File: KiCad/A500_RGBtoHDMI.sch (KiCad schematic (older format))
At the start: 3 parts, among them J1 Conn_02x20_Odd_Even, U1 Denise_MB_pins, U2 Denise_SocketOnAdapter

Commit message: improved design
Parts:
- U1: value Denise_MB_pins -> Denise_MB_PinHeader
- U2: value Denise_SocketOnAdapter -> Denise_MB_PinSocket
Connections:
- net D6: now reaches U1.1 (D6)
- net D6: now also U2.1 (D6)
- net D5: now reaches U1.2 (D5)
- net D5: now also U2.2 (D5)
- net D4: now reaches U1.3 (D4)
- net D4: now also U2.3 (D4)
- net D3: now reaches U1.4 (D3)
- net D3: now also U2.4 (D3)
- net D2: now reaches U1.5 (D2)
- net D2: now also U2.5 (D2)
- net D1: now reaches U1.6 (D1)
- net D1: now also U2.6 (D1)
- net D0: now reaches U1.7 (D0)
- net D0: now also U2.7 (D0)
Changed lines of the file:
@@
 P 2950 3100
 F 0 "U1" H 2950 4665 50  0000 C CNN
-F 1 "Denise_MB_pins" H 2950 4574 50  0000 C CNN
+F 1 "Denise_MB_PinHeader" H 2950 4574 50  0000 C CNN
 F 2 "Package_DIP:DIP-48_W15.24mm_LongPads" H 2900 1600 50  0001 C CNN
 F 3 "" H 2900 1600 50  0001 C CNN
@@
 $Comp
 L A500_RGBtoHDMI:Denise U2
-U 1 1 623C9B51
-P 4950 3100
-F 0 "U2" H 4950 4665 50  0000 C CNN
-F 1 "Denise_SocketOnAdapter" H 4950 4574 50  0000 C CNN
-F 2 "Package_DIP:DIP-48_W15.24mm_Socket_LongPads" H 4900 1600 50  0001 C CNN
-F 3 "" H 4900 1600 50  0001 C CNN
-	1    4950 3100
+U 1 1 623E379A
+P 4700 3100
+F 0 "U2" H 4700 4665 50  0000 C CNN
+F 1 "Denise_MB_PinSocket" H 4700 4574 50  0000 C CNN
+F 2 "Package_DIP:DIP-48_W15.24mm_Socket_LongPads" H 4650 1600 50  0001 C CNN
+F 3 "" H 4650 1600 50  0001 C CNN
+	1    4700 3100
 	1    0    0    -1
 $EndComp
+Text GLabel 2400 1800 0    50   BiDi ~ 0
+D6
+Text GLabel 4150 1800 0    50   BiDi ~ 0
+D6
+Text GLabel 2400 1900 0    50   BiDi ~ 0
+D5
+Text GLabel 4150 1900 0    50   BiDi ~ 0
+D5
+Text GLabel 2400 2000 0    50   BiDi ~ 0
+D4
+Text GLabel 2400 2100 0    50   BiDi ~ 0
+D3
+Text GLabel 2400 2200 0    50   BiDi ~ 0
+D2
+Text GLabel 2400 2300 0    50   BiDi ~ 0
+D1
+Text GLabel 2400 2400 0    50   BiDi ~ 0
+D0
+Text GLabel 4150 2000 0    50   BiDi ~ 0
+D4
+Text GLabel 4150 2100 0    50   BiDi ~ 0
+D3
+Text GLabel 4150 2200 0    50   BiDi ~ 0
+D2
+Text GLabel 4150 2300 0    50   BiDi ~ 0
+D1
+Text GLabel 4150 2400 0    50   BiDi ~ 0
+D0
 $EndSCHEMATC

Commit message: more routing
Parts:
- U2: value Denise_MB_PinSocket -> Denise_Socket
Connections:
- net +5V: now also U1.19 (VCC), U2.19 (VCC); no longer J1.1 (Pin_1)
- net GND: now also U1.37 (GND), U2.37 (GND); no longer J1.2 (Pin_2)
- net RGA8: now reaches U1.10 (RGA8)
- net RGA8: now also U2.10 (RGA8)
- net RGA7: now reaches U1.11 (RGA7)
- net RGA7: now also U2.11 (RGA7)
- net RGA6: now reaches U1.12 (RGA6)
- net RGA6: now also U2.12 (RGA6)
- net RGA5: now reaches U1.13 (RGA5)
- net RGA5: now also U2.13 (RGA5)
- net RGA4: now reaches U1.14 (RGA4)
- net RGA4: now also U2.14 (RGA4)
- net RGA3: now reaches U1.15 (RGA3)
- net RGA3: now also U2.15 (RGA3)
- net RGA2: now reaches U1.16 (RGA2)
- net RGA2: now also U2.16 (RGA2)
- net RGA1: now reaches U1.17 (RGA1)
- net RGA1: now also U2.17 (RGA1)
- net BURST: now reaches U1.18 (BURST)
- net BURST: now also U2.18 (BURST)
- net R0: now reaches U1.20 (R0)
- net R0: now also U2.20 (R0)
- net R1: now reaches U1.21 (R1)
- net R1: now also U2.21 (R1)
- net R2: now reaches U1.22 (R2)
- net R2: now also U2.22 (R2)
- net R3: now reaches U1.23 (R3)
- net R3: now also U2.23 (R3)
- net B0: now reaches U1.24 (B0)
- net B0: now also U2.24 (B0)
- net B1: now reaches U1.25 (B1)
- net B1: now also U2.25 (B1)
- net B2: now reaches U1.26 (B2)
- net B2: now also U2.26 (B2)
- net B3: now reaches U1.27 (B3)
- net B3: now also U2.27 (B3)
- net G0: now reaches U1.28 (G0)
- net G0: now also U2.28 (G0)
- net G1: now reaches U1.29 (G1)
- net G1: now also U2.29 (G1)
- net G2: now reaches U1.30 (G2)
- net G2: now also U2.30 (G2)
- net G3: now reaches U1.31 (G3)
- net G3: now also U2.31 (G3)
- net CBL: now reaches U1.32 (BLANK)
- net CBL: now also U2.32 (BLANK)
- net ZD: now reaches U1.33 (PIXELSW)
- net ZD: now also U2.33 (PIXELSW)
- net CDAC: now reaches U1.34 (~CDAC)
- net CDAC: now also U2.34 (~CDAC)
- net C7M: now reaches U1.35 (7M)
- net C7M: now also U2.35 (7M)
- net CCK: now reaches U1.36 (CCK)
- net CCK: now also U2.36 (CCK)
- net M0V: now reaches U1.38 (M0V)
- net M0V: now also U2.38 (M0V)
- net M1V: now reaches U1.39 (M1V)
- net M1V: now also U2.39 (M1V)
- net D15: now reaches U1.40 (D15)
- net D15: now also U2.40 (D15)
- net D14: now reaches U1.41 (D14)
- net D14: now also U2.41 (D14)
- net D13: now reaches U1.42 (D13)
- net D13: now also U2.42 (D13)
- net D12: now reaches U1.43 (D12)
- net D12: now also U2.43 (D12)
- net D11: now reaches U1.44 (D11)
- net D11: now also U2.44 (D11)
- net D10: now reaches U1.45 (D10)
- net D10: now also U2.45 (D10)
- net D9: now reaches U1.46 (D9)
- net D9: now also U2.46 (D9)
- net D8: now reaches U1.47 (D8)
- net D8: now also U2.47 (D8)
- net D7: now reaches U1.48 (D7)
- net D7: now also U2.48 (D7)
- net M1H: now reaches U1.8 (M1H)
- net M1H: now also U2.8 (M1H)
- net M0H: now reaches U1.9 (M0H)
- net M0H: now also U2.9 (M0H)
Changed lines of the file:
@@
 	1    0    0    -1
 $EndComp
-Text GLabel 6650 2150 0    50   Input ~ 0
-VCC
-Text GLabel 7150 2150 2    50   Input ~ 0
-GND
 $Comp
 L A500_RGBtoHDMI:Denise U1
@@
 P 4700 3100
 F 0 "U2" H 4700 4665 50  0000 C CNN
-F 1 "Denise_MB_PinSocket" H 4700 4574 50  0000 C CNN
+F 1 "Denise_Socket" H 4700 4574 50  0000 C CNN
 F 2 "Package_DIP:DIP-48_W15.24mm_Socket_LongPads" H 4650 1600 50  0001 C CNN
 F 3 "" H 4650 1600 50  0001 C CNN
@@
 Text GLabel 4150 2400 0    50   BiDi ~ 0
 D0
+Text GLabel 2400 2550 0    50   Output ~ 0
+M1H
+Text GLabel 2400 2650 0    50   Output ~ 0
+M0H
+Text GLabel 4150 2550 0    50   Input ~ 0
+M1H
+Text GLabel 4150 2650 0    50   Input ~ 0
+M0H
+Text GLabel 2400 3000 0    50   Output ~ 0
+RGA6
+Text GLabel 2400 3100 0    50   Output ~ 0
+RGA5
+Text GLabel 2400 3200 0    50   Output ~ 0
+RGA4
+Text GLabel 2400 3300 0    50   Output ~ 0
+RGA3
+Text GLabel 2400 3400 0    50   Output ~ 0
+RGA2
+Text GLabel 2400 3500 0    50   Output ~ 0
+RGA1
+Text GLabel 2400 2900 0    50   Output ~ 0
+RGA7
+Text GLabel 2400 2800 0    50   Output ~ 0
+RGA8
+Text GLabel 4150 3000 0    50   Input ~ 0
+RGA6
+Text GLabel 4150 3100 0    50   Input ~ 0
+RGA5
+Text GLabel 4150 3200 0    50   Input ~ 0
+RGA4
+Text GLabel 4150 3300 0    50   Input ~ 0
+RGA3
+Text GLabel 4150 3400 0    50   Input ~ 0
+RGA2
+Text GLabel 4150 3500 0    50   Input ~ 0
+RGA1
+Text GLabel 4150 2900 0    50   Input ~ 0
+RGA7
+Text GLabel 4150 2800 0    50   Input ~ 0
+RGA8
+Text GLabel 4150 3650 0    50   Output ~ 0
+BURST
+Text GLabel 2400 3650 0    50   Input ~ 0
+BURST
+Text GLabel 2400 3800 0    50   Input ~ 0
+VCC
+Text GLabel 4150 3800 0    50   Input ~ 0
+VCC
+Text GLabel 2400 4050 0    50   Input ~ 0
+R1
+Text GLabel 2400 3950 0    50   Input ~ 0
+R0
+Text GLabel 2400 4250 0    50   Input ~ 0
+R3
+Text GLabel 2400 4150 0    50   Input ~ 0
+R2
+Text GLabel 2400 4350 0    50   Input ~ 0
+B0
+Text GLabel 4150 4050 0    50   Output ~ 0
+R1
+Text GLabel 4150 3950 0    50   Output ~ 0
+R0
+Text GLabel 4150 4250 0    50   Output ~ 0
+R3
+Text GLabel 4150 4150 0    50   Output ~ 0
+R2
+Text GLabel 4150 4350 0    50   Output ~ 0
+B0
+Text GLabel 3500 3950 2    50   Input ~ 0
+G1
+Text GLabel 3500 4050 2    50   Input ~ 0
+G0
+Text GLabel 3500 4250 2    50   Input ~ 0
+B2
+Text GLabel 3500 4150 2    50   Input ~ 0
+B3
+Text GLabel 3500 4350 2    50   Input ~ 0
+B1
+Text GLabel 3500 3750 2    50   Input ~ 0
+G3
+Text GLabel 3500 3850 2    50   Input ~ 0
+G2
+Text GLabel 5250 3950 2    50   Output ~ 0
+G1
+Text GLabel 5250 4050 2    50   Output ~ 0
+G0
+Text GLabel 5250 4250 2    50   Output ~ 0
+B2
+Text GLabel 5250 4150 2    50   Output ~ 0
+B3
+Text GLabel 5250 4350 2    50   Output ~ 0
+B1
+Text GLabel 5250 3750 2    50   Output ~ 0
+G3
+Text GLabel 5250 3850 2    50   Output ~ 0
+G2
+Text GLabel 5250 3550 2    50   Input ~ 0
+CBL
+Text GLabel 3500 3550 2    50   Output ~ 0
+CBL
+Text GLabel 5250 3450 2    50   Output ~ 0
+ZD
+Text GLabel 3500 3450 2    50   Input ~ 0
+ZD
+Text GLabel 5250 3350 2    50   Input ~ 0
+CDAC
+Text GLabel 3500 3350 2    50   Output ~ 0
+CDAC
+Text GLabel 3500 3250 2    50   Output ~ 0
+C7M
+Text GLabel 5250 3250 2    50   Input ~ 0
+C7M
+Text GLabel 3500 3150 2    50   Output ~ 0
+CCK
+Text GLabel 5250 3150 2    50   Input ~ 0
+CCK
+Text GLabel 3500 3000 2    50   Input ~ 0
+GND
+Text GLabel 5250 3000 2    50   Input ~ 0
+GND
+Text GLabel 3500 2750 2    50   Output ~ 0
+M1V
+Text GLabel 3500 2850 2    50   Output ~ 0
+M0V
+Text GLabel 5250 2750 2    50   Input ~ 0
+M1V
+Text GLabel 5250 2850 2    50   Input ~ 0
+M0V
+Text GLabel 3500 1800 2    50   BiDi ~ 0
+D7
+Text GLabel 3500 1900 2    50   BiDi ~ 0
+D8
+Text GLabel 3500 2000 2    50   BiDi ~ 0
+D9
+Text GLabel 3500 2100 2    50   BiDi ~ 0
+D10
+Text GLabel 3500 2200 2    50   BiDi ~ 0
+D11
+Text GLabel 3500 2300 2    50   BiDi ~ 0
+D12
+Text GLabel 3500 2400 2    50   BiDi ~ 0
+D13
+Text GLabel 3500 2500 2    50   BiDi ~ 0
+D14
+Text GLabel 3500 2600 2    50   BiDi ~ 0
+D15
+Text GLabel 5250 1800 2    50   BiDi ~ 0
+D7
+Text GLabel 5250 1900 2    50   BiDi ~ 0
+D8
+Text GLabel 5250 2000 2    50   BiDi ~ 0
+D9
+Text GLabel 5250 2100 2    50   BiDi ~ 0
+D10
+Text GLabel 5250 2200 2    50   BiDi ~ 0
+D11
+Text GLabel 5250 2300 2    50   BiDi ~ 0
+D12
+Text GLabel 5250 2400 2    50   BiDi ~ 0
+D13
+Text GLabel 5250 2500 2    50   BiDi ~ 0
+D14
+Text GLabel 5250 2600 2    50   BiDi ~ 0
+D15
 $EndSCHEMATC

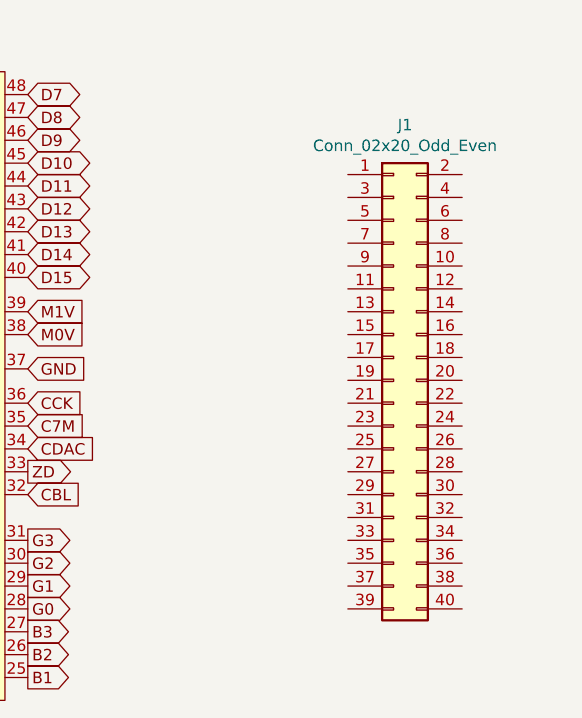
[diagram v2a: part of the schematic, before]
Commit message: added networks to Pi-header
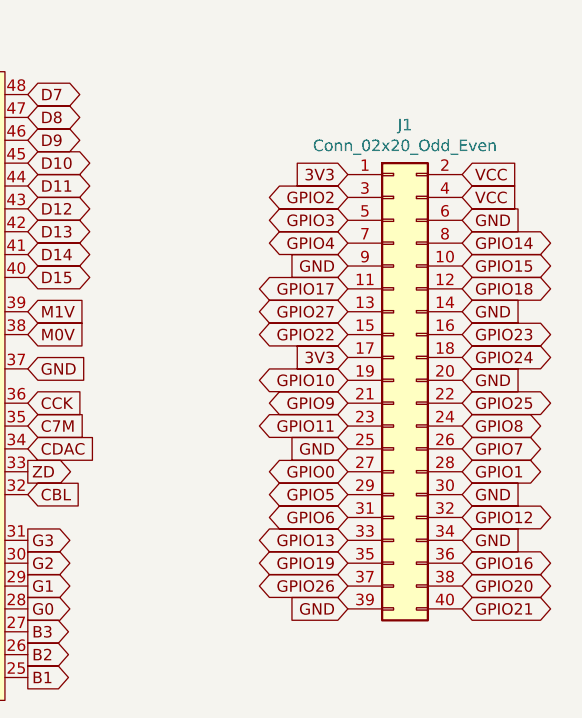
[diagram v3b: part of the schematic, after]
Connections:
- net +5V: now also J1.2 (Pin_2), J1.4 (Pin_4)
- net GND: now also J1.14 (Pin_14), J1.20 (Pin_20), J1.25 (Pin_25), J1.30 (Pin_30), J1.34 (Pin_34), J1.39 (Pin_39), J1.6 (Pin_6), J1.9 (Pin_9)
- net 3V3: now reaches J1.1 (Pin_1)
- net 3V3: now also J1.17 (Pin_17)
- net GPIO15: now reaches J1.10 (Pin_10)
- net GPIO17: now reaches J1.11 (Pin_11)
- net GPIO18: now reaches J1.12 (Pin_12)
- net GPIO27: now reaches J1.13 (Pin_13)
- net GPIO22: now reaches J1.15 (Pin_15)
- net GPIO23: now reaches J1.16 (Pin_16)
- net GPIO24: now reaches J1.18 (Pin_18)
- net GPIO10: now reaches J1.19 (Pin_19)
- net GPIO9: now reaches J1.21 (Pin_21)
- net GPIO25: now reaches J1.22 (Pin_22)
- net GPIO11: now reaches J1.23 (Pin_23)
- net GPIO8: now reaches J1.24 (Pin_24)
- net GPIO7: now reaches J1.26 (Pin_26)
- net GPIO0: now reaches J1.27 (Pin_27)
- net GPIO1: now reaches J1.28 (Pin_28)
- net GPIO5: now reaches J1.29 (Pin_29)
- net GPIO2: now reaches J1.3 (Pin_3)
- net GPIO6: now reaches J1.31 (Pin_31)
- net GPIO12: now reaches J1.32 (Pin_32)
- net GPIO13: now reaches J1.33 (Pin_33)
- net GPIO19: now reaches J1.35 (Pin_35)
- net GPIO16: now reaches J1.36 (Pin_36)
- net GPIO26: now reaches J1.37 (Pin_37)
- net GPIO20: now reaches J1.38 (Pin_38)
- net GPIO21: now reaches J1.40 (Pin_40)
- net GPIO3: now reaches J1.5 (Pin_5)
- net GPIO4: now reaches J1.7 (Pin_7)
- net GPIO14: now reaches J1.8 (Pin_8)
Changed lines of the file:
@@
 Text GLabel 5250 2600 2    50   BiDi ~ 0
 D15
+Text GLabel 7150 2150 2    50   Input ~ 0
+VCC
+Text GLabel 7150 2250 2    50   Input ~ 0
+VCC
+Text GLabel 6650 2150 0    50   Input ~ 0
+3V3
+Text GLabel 7150 2350 2    50   Input ~ 0
+GND
+Text GLabel 6650 2550 0    50   Input ~ 0
+GND
+Text GLabel 7150 2750 2    50   Input ~ 0
+GND
+Text GLabel 7150 3050 2    50   Input ~ 0
+GND
+Text GLabel 6650 3350 0    50   Input ~ 0
+GND
+Text GLabel 7150 3550 2    50   Input ~ 0
+GND
+Text GLabel 7150 3750 2    50   Input ~ 0
+GND
+Text GLabel 6650 4050 0    50   Input ~ 0
+GND
+Text GLabel 6650 2250 0    50   BiDi ~ 0
+GPIO2
+Text GLabel 6650 2350 0    50   BiDi ~ 0
+GPIO3
+Text GLabel 6650 2450 0    50   BiDi ~ 0
+GPIO4
+Text GLabel 7150 2450 2    50   BiDi ~ 0
+GPIO14
+Text GLabel 7150 2550 2    50   BiDi ~ 0
+GPIO15
+Text GLabel 6650 2650 0    50   BiDi ~ 0
+GPIO17
+Text GLabel 7150 2650 2    50   BiDi ~ 0
+GPIO18
+Text GLabel 6650 2750 0    50   BiDi ~ 0
+GPIO27
+Text GLabel 6650 2850 0    50   BiDi ~ 0
+GPIO22
+Text GLabel 7150 2850 2    50   BiDi ~ 0
+GPIO23
+Text GLabel 7150 2950 2    50   BiDi ~ 0
+GPIO24
+Text GLabel 6650 2950 0    50   Input ~ 0
+3V3
+Text GLabel 6650 3050 0    50   BiDi ~ 0
+GPIO10
+Text GLabel 6650 3150 0    50   BiDi ~ 0
+GPIO9
+Text GLabel 6650 3250 0    50   BiDi ~ 0
+GPIO11
+Text GLabel 7150 3150 2    50   BiDi ~ 0
+GPIO25
+Text GLabel 7150 3250 2    50   BiDi ~ 0
+GPIO8
+Text GLabel 7150 3350 2    50   BiDi ~ 0
+GPIO7
+Text GLabel 6650 3450 0    50   BiDi ~ 0
+GPIO0
+Text GLabel 7150 3450 2    50   BiDi ~ 0
+GPIO1
+Text GLabel 6650 3550 0    50   BiDi ~ 0
+GPIO5
+Text GLabel 6650 3650 0    50   BiDi ~ 0
+GPIO6
+Text GLabel 7150 3650 2    50   BiDi ~ 0
+GPIO12
+Text GLabel 6650 3750 0    50   BiDi ~ 0
+GPIO13
+Text GLabel 6650 3850 0    50   BiDi ~ 0
+GPIO19
+Text GLabel 7150 3850 2    50   BiDi ~ 0
+GPIO16
+Text GLabel 6650 3950 0    50   BiDi ~ 0
+GPIO26
+Text GLabel 7150 3950 2    50   BiDi ~ 0
+GPIO20
+Text GLabel 7150 4050 2    50   BiDi ~ 0
+GPIO21
 $EndSCHEMATC

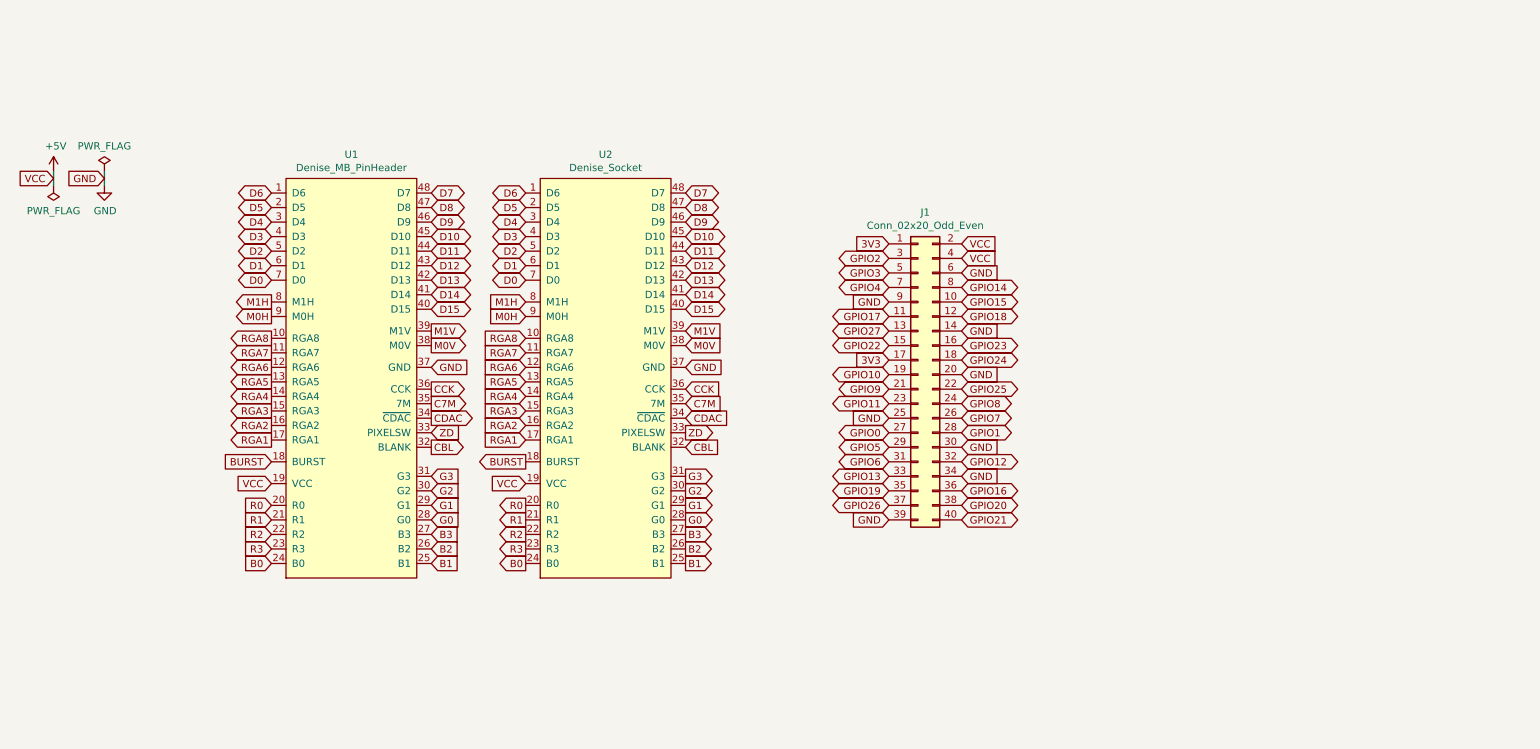
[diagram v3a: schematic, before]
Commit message: added CPLD XC9572XL-VQ64 and did more layout and routing
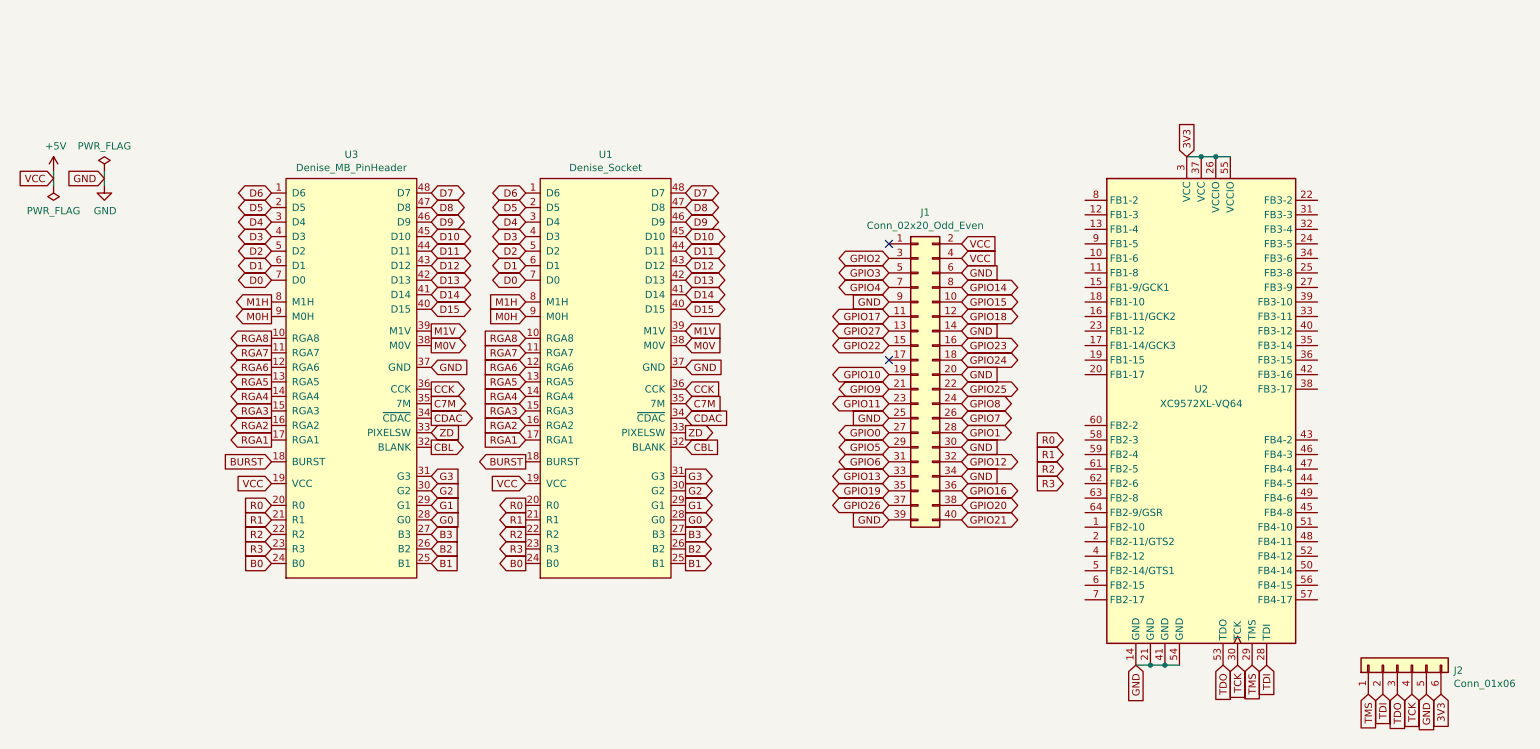
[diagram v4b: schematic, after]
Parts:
- added J2: Conn_01x06, Connector_PinHeader_2.54mm:PinHeader_1x06_P2.54mm_Vertical, symbol Connector_Generic:Conn_01x06
- added U2: XC9572XL-VQ64, Package_QFP:TQFP-64_10x10mm_P0.5mm, symbol A500_RGBtoHDMI:XC9572XL-VQ64
- renumbered U2 to U1, U1 to U3
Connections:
- net 3V3: now also J2.6 (Pin_6), U2.26 (VCCIO), U2.3 (VCC), U2.37 (VCC), U2.55 (VCCIO); no longer J1.1 (Pin_1), J1.17 (Pin_17)
- net GND: now also J2.5 (Pin_5), U2.14 (GND), U2.21 (GND), U2.41 (GND), U2.54 (GND)
- new net TCK: J2.4 (Pin_4), U2.30 (TCK)
- new net TDI: J2.2 (Pin_2), U2.28 (TDI)
- new net TDO: J2.3 (Pin_3), U2.53 (TDO)
- new net TMS: J2.1 (Pin_1), U2.29 (TMS)
- no-connect marks 0 -> 2
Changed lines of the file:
@@
 $EndComp
 $Comp
-L A500_RGBtoHDMI:Denise U1
+L A500_RGBtoHDMI:Denise U3
 U 1 1 623BE5C5
 P 2950 3100
-F 0 "U1" H 2950 4665 50  0000 C CNN
+F 0 "U3" H 2950 4665 50  0000 C CNN
 F 1 "Denise_MB_PinHeader" H 2950 4574 50  0000 C CNN
 F 2 "Package_DIP:DIP-48_W15.24mm_LongPads" H 2900 1600 50  0001 C CNN
@@
 $EndComp
 $Comp
-L A500_RGBtoHDMI:Denise U2
+L A500_RGBtoHDMI:Denise U1
 U 1 1 623E379A
 P 4700 3100
-F 0 "U2" H 4700 4665 50  0000 C CNN
+F 0 "U1" H 4700 4665 50  0000 C CNN
 F 1 "Denise_Socket" H 4700 4574 50  0000 C CNN
 F 2 "Package_DIP:DIP-48_W15.24mm_Socket_LongPads" H 4650 1600 50  0001 C CNN
@@
 Text GLabel 7150 2250 2    50   Input ~ 0
 VCC
-Text GLabel 6650 2150 0    50   Input ~ 0
-3V3
 Text GLabel 7150 2350 2    50   Input ~ 0
 GND
@@
 Text GLabel 7150 2950 2    50   BiDi ~ 0
 GPIO24
-Text GLabel 6650 2950 0    50   Input ~ 0
-3V3
 Text GLabel 6650 3050 0    50   BiDi ~ 0
 GPIO10
@@
 Text GLabel 7150 4050 2    50   BiDi ~ 0
 GPIO21
+$Comp
+L A500_RGBtoHDMI:XC9572XL-VQ64 U2
+U 1 1 623D7A48
+P 8800 3250
+F 0 "U2" H 8800 3350 50  0000 C CNN
+F 1 "XC9572XL-VQ64" H 8800 3250 50  0000 C CNN
+F 2 "Package_QFP:TQFP-64_10x10mm_P0.5mm" V 9100 3150 50  0001 C CNN
+F 3 "http://www.xilinx.com/support/documentation/data_sheets/ds057.pdf" H 8800 3250 50  0001 C CNN
+	1    8800 3250
+	1    0    0    -1
+$EndComp
+Text GLabel 8350 5050 3    50   Input ~ 0
+GND
+Wire Wire Line
+	8350 5050 8450 5050
+Connection ~ 8450 5050
+Wire Wire Line
+	8450 5050 8550 5050
+Connection ~ 8550 5050
+Wire Wire Line
+	8550 5050 8650 5050
+$Comp
+L Connector_Generic:Conn_01x06 J2
+U 1 1 6241CCF9
+P 10150 5050
+F 0 "J2" V 10114 4662 50  0000 R CNN
+F 1 "Conn_01x06" V 10023 4662 50  0000 R CNN
+F 2 "Connector_PinHeader_2.54mm:PinHeader_1x06_P2.54mm_Vertical" H 10150 5050 50  0001 C CNN
+F 3 "~" H 10150 5050 50  0001 C CNN
+	1    10150 5050
+	0    -1   -1   0
+$EndComp
+Text GLabel 9950 5250 3    50   Input ~ 0
+TMS
+Text GLabel 10050 5250 3    50   Input ~ 0
+TDI
+Text GLabel 10150 5250 3    50   Input ~ 0
+TDO
+Text GLabel 10250 5250 3    50   Input ~ 0
+TCK
+Text GLabel 10350 5250 3    50   Input ~ 0
+GND
+Text GLabel 10450 5250 3    50   Input ~ 0
+3V3
+Text GLabel 8950 5050 3    50   Input ~ 0
+TDO
+Text GLabel 9050 5050 3    50   Input ~ 0
+TCK
+Text GLabel 9150 5050 3    50   Input ~ 0
+TMS
+Text GLabel 9250 5050 3    50   Input ~ 0
+TDI
+NoConn ~ 6650 2150
+NoConn ~ 6650 2950
+Text GLabel 8700 1550 1    50   Input ~ 0
+3V3
+Wire Wire Line
+	8700 1550 8800 1550
+Connection ~ 8800 1550
+Wire Wire Line
+	8800 1550 8900 1550
+Connection ~ 8900 1550
+Wire Wire Line
+	8900 1550 9000 1550
+Text GLabel 7850 3600 0    50   Input ~ 0
+R1
+Text GLabel 7850 3500 0    50   Input ~ 0
+R0
+Text GLabel 7850 3800 0    50   Input ~ 0
+R3
+Text GLabel 7850 3700 0    50   Input ~ 0
+R2
 $EndSCHEMATC
